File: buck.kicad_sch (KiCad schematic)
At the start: 0 parts

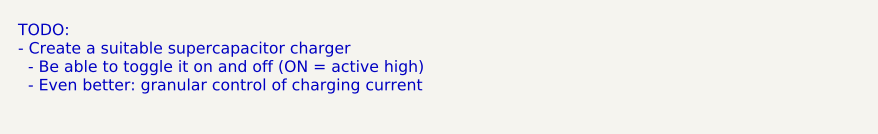
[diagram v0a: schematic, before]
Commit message: Add note about synchronous boost/buck needed
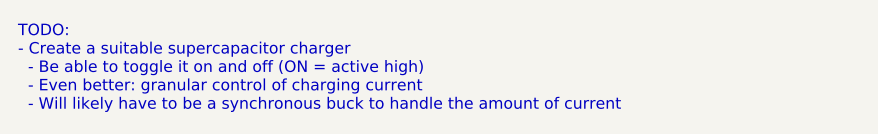
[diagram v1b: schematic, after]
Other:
- note added: "TODO: - Create a suitable supercapacitor charger - Be able to toggle it on and off (ON = active high) - Even better: granular control of charging current - Will likely have to be a synchronous buck to handle the amount of current"
- note removed: "TODO: - Create a suitable supercapacitor charger - Be able to toggle it on and off (ON = active high) - Even better: granular control of charging current"
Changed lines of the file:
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@@
 		(comment 1 "Robomaster")
 	)
-	(text "TODO:\n- Create a suitable supercapacitor charger\n  - Be able to toggle it on and off (ON = active high)\n  - Even better: granular control of charging current"
+	(text "TODO:\n- Create a suitable supercapacitor charger\n  - Be able to toggle it on and off (ON = active high)\n  - Even better: granular control of charging current\n  - Will likely have to be a synchronous buck to handle the amount of current"
 		(exclude_from_sim no)
 		(at 132.08 95.25 0)

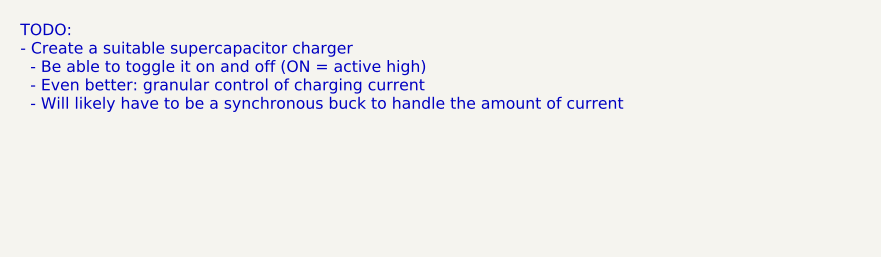
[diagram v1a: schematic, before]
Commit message: Added in & out data from each subsheet
For more details, please contact @leftisttachyon on Discord
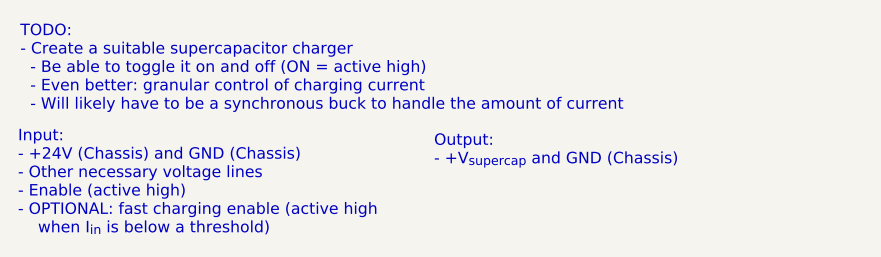
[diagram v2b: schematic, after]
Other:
- note added: "Input: - +24V (Chassis) and GND (Chassis) - Other necessary voltage lines - Enable (active high) - OPTIONAL: fast charging enable (active high when I_{in} is below a threshold)"
- note added: "Output: - +V_{supercap} and GND (Chassis)"
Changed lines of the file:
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@@
+		)
+	)
+	(text "Input:\n- +24V (Chassis) and GND (Chassis)\n- Other necessary voltage lines\n- Enable (active high)\n- OPTIONAL: fast charging enable (active high \n    when I_{in} is below a threshold)"
+		(exclude_from_sim no)
+		(at 131.826 106.934 0)
+		(effects
+			(font
+				(size 1.27 1.27)
+			)
+			(justify left top)
+		)
+	)
+	(text "Output:\n- +V_{supercap} and GND (Chassis)"
+		(exclude_from_sim no)
+		(at 178.054 107.442 0)
+		(effects
+			(font
+				(size 1.27 1.27)
+			)
+			(justify left top)
 		)
 	)

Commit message: Completed first version of housekeeping supplies
+5V and +3V3 from mini PC +24V
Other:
- company: UT Stampede -> UT Robomaster
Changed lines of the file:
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@@
 	(paper "A4")
 	(title_block
-		(date "2024-10-18")
+		(date "2024-11-15")
 		(rev "1")
-		(company "UT Stampede")
+		(company "UT Robomaster")
 		(comment 1 "Robomaster")
 	)

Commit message: Finishing buck charger
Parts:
- added C27: 0.1u, Capacitor_SMD:C_0603_1608Metric_Pad1.08x0.95mm_HandSolder, symbol Device:C_Small
- added C28, C31: 1u, Capacitor_SMD:C_0603_1608Metric_Pad1.08x0.95mm_HandSolder, symbol Device:C_Small
- added C29: 1u, Capacitor_SMD:C_0603_1608Metric_Pad1.08x0.95mm_HandSolder, symbol Device:C
- added C30: 2.2u, symbol Device:C_Polarized
- added C32, C33: 10u, symbol Device:C_Polarized
- added C34, C35: 0.1u, Capacitor_SMD:C_0603_1608Metric_Pad1.08x0.95mm_HandSolder, symbol Device:C
- added C36, C37: C, symbol Device:C_Polarized
- added C38: C, Capacitor_SMD:C_0603_1608Metric_Pad1.08x0.95mm_HandSolder, symbol Device:C
- added D3, D4: LED, LED_SMD:LED_0603_1608Metric_Pad1.05x0.95mm_HandSolder, symbol Device:LED
- added D5: BAT54J, Diode_SMD:D_SOD-323F, symbol Diode:BAT54J
- added L4: L, symbol Device:L
- added Q2, Q3: Q_NMOS_SGD, symbol Device:Q_NMOS_SGD
- added R17, R32, R35, R36: R, Resistor_SMD:R_0603_1608Metric_Pad0.98x0.95mm_HandSolder, symbol Device:R
- added R33: 6.8, Resistor_SMD:R_0603_1608Metric_Pad0.98x0.95mm_HandSolder, symbol Device:R
- added R34: 10m, Resistor_SMD:R_0603_1608Metric_Pad0.98x0.95mm_HandSolder, symbol Device:R
- added U9: BQ24640, ! Robomaster ICs:QFN50P350X350X100-17N-D, symbol ! Robomaster ICs:BQ24640
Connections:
- new net BTST: C27.1, D5.1 (K), U9.16 (BTST)
- new net CHARGE_EN: U9.2 (CE)
- new net GNDPWR: C28.2, C29.2, C30.2, C31.2, C32.2, C33.2, C34.2, C36.2, C37.2, Q3.1 (S), R36.2, U9.11 (GND), U9.17 (PAD)
- new net HIDRV: Q2.2 (G), U9.15 (HIDRV)
- new net IN: C30.1, C32.1, C33.1, Q2.3 (D), R17.1, R32.1, R33.1
- new net ISET: U9.7 (ISET)
- new net LODRV: Q3.2 (G), U9.13 (LODRV)
- new net OUT: C35.2, C36.1, C37.1, C38.1, R34.1, R35.1, U9.9 (SRN)
- new net PH: C27.2, L4.1, Q2.1 (S), Q3.3 (D), U9.14 (PH)
- new net REGN: C28.1, D5.2 (A), U9.12 (REGN)
- new net SRP: C34.1, C35.1, L4.2, R34.2, U9.10 (SRP)
- new net STAT: D3.1 (K), U9.3 (STAT)
- new net STAT_D: D3.2 (A), R17.2
- new net TS: U9.4 (TS)
- new net VCC: C29.1, R33.2, U9.1 (VCC)
- new net VFB: C38.2, R35.2, R36.1, U9.8 (VFB)
- new net VREF: C31.1, U9.6 (VREF)
- new net ~{PG}: D4.1 (K), U9.5 (~{PG})
- new net ~{PG}_D: D4.2 (A), R32.2
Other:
- note added: "Current sensing"
- note added: "Feedback network"
- note added: "High ESR"
- note added: "Low ESR"
- note added: "Output caps"
- note added: "Power path"
- note added: "Status LEDs for charging & current draw"
- note added: "Supercap Charging Controller"
- note added: "Totem pole"
- note added: "VCC Input Filtering"

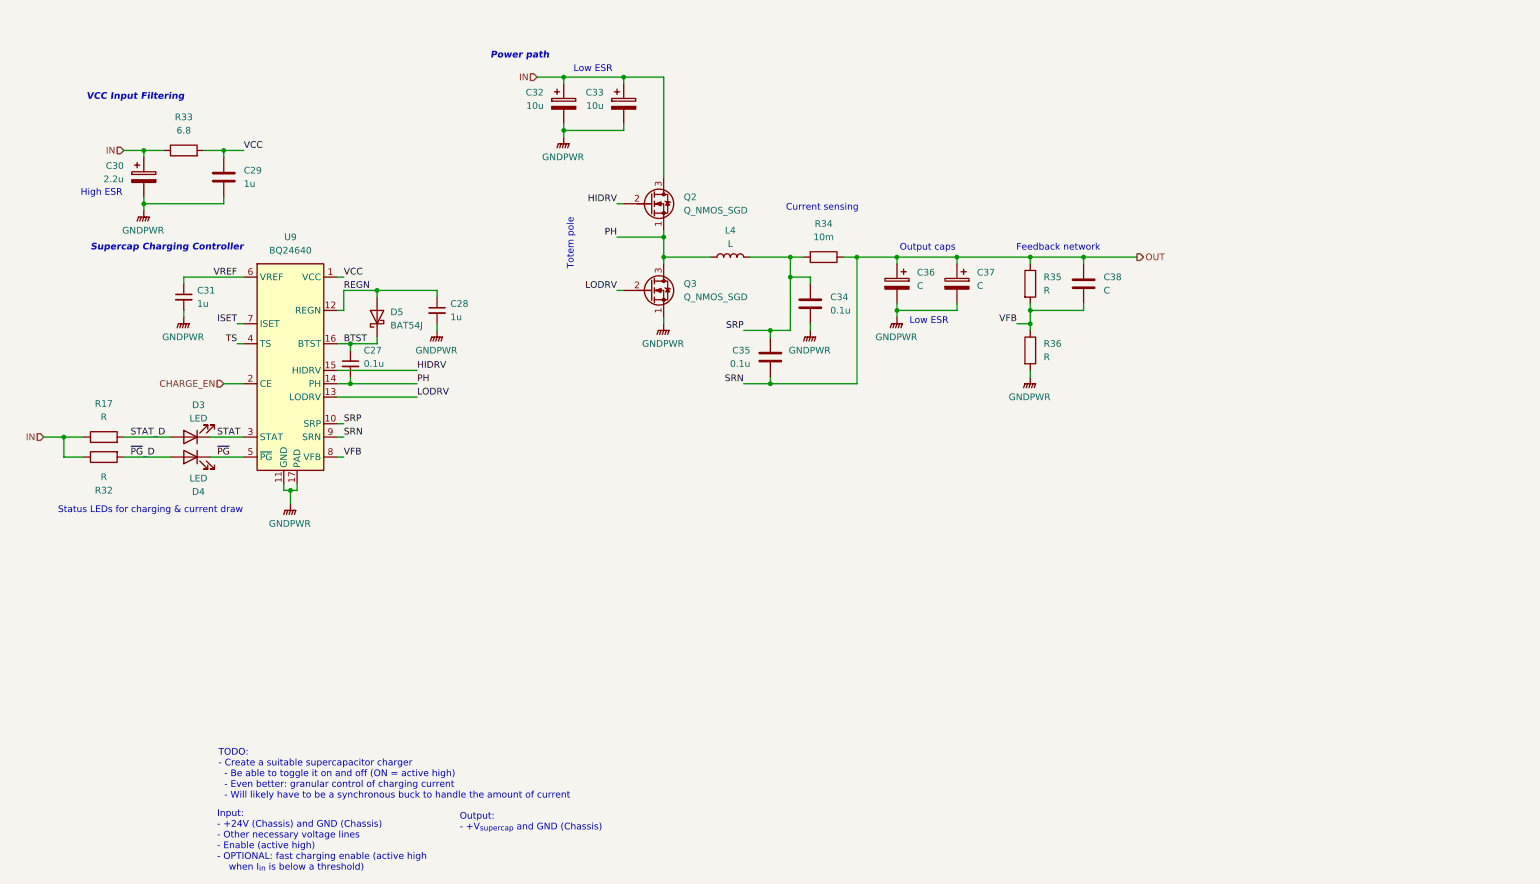
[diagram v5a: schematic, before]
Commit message: Define feedback networks
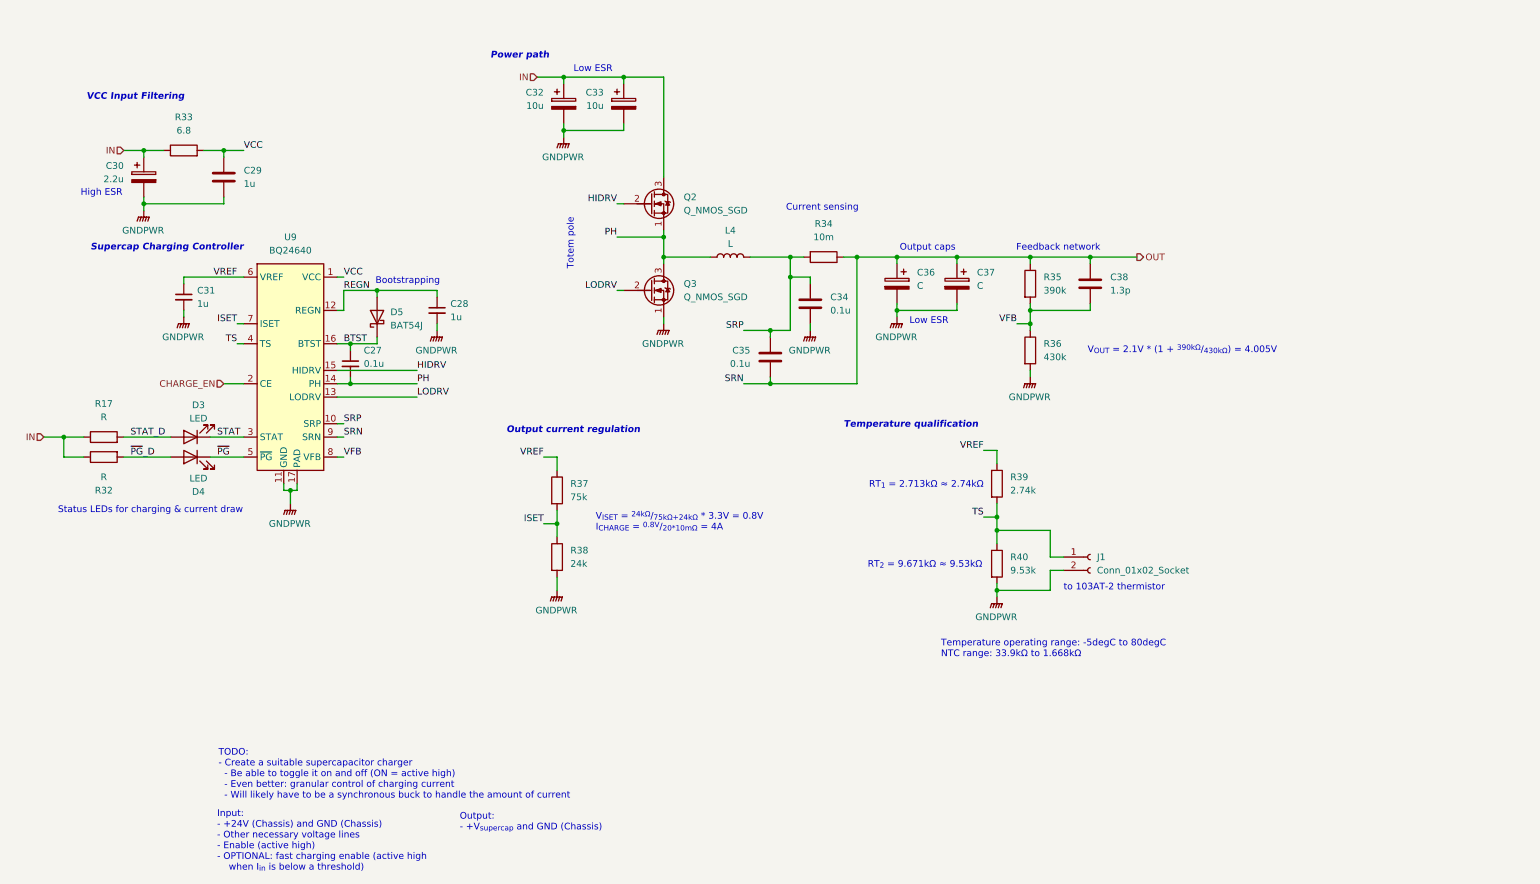
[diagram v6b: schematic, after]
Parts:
- added J1: Conn_01x02_Socket, Connector_PinSocket_2.00mm:PinSocket_1x02_P2.00mm_Vertical, symbol Connector:Conn_01x02_Socket
- added R37: 75k, Resistor_SMD:R_0603_1608Metric_Pad0.98x0.95mm_HandSolder, symbol Device:R
- added R38: 24k, Resistor_SMD:R_0603_1608Metric_Pad0.98x0.95mm_HandSolder, symbol Device:R
- added R39: 2.74k, Resistor_SMD:R_0603_1608Metric_Pad0.98x0.95mm_HandSolder, symbol Device:R
- added R40: 9.53k, Resistor_SMD:R_0603_1608Metric_Pad0.98x0.95mm_HandSolder, symbol Device:R
- C38: value C -> 1.3p
- R35: value R -> 390k
- R36: value R -> 430k
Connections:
- net GNDPWR: now also J1.2 (Pin_2), R38.2, R40.2
- net ISET: now also R37.2, R38.1
- net TS: now also J1.1 (Pin_1), R39.2, R40.1
- net VREF: now also R37.1, R39.1
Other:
- note added: "Bootstrapping"
- note added: "Output current regulation"
- note added: "RT_{1} = 2.713kΩ ≈ 2.74kΩ"
- note added: "RT_{2} = 9.671kΩ ≈ 9.53kΩ"
- note added: "Temperature operating range: -5degC to 80degC NTC range: 33.9kΩ to 1.668kΩ"
- note added: "Temperature qualification"
- note added: "V_{ISET} = ^{24kΩ}/_{75kΩ+24kΩ} * 3.3V = 0.8V I_{CHARGE} = ^{0.8V}/_{20*10mΩ} = 4A"
- note added: "V_{OUT} = 2.1V * (1 + ^{390kΩ}/_{430kΩ}) = 4.005V"
- note added: "to 103AT-2 thermistor"
- moved on the sheet: C38

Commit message: Finish up buck
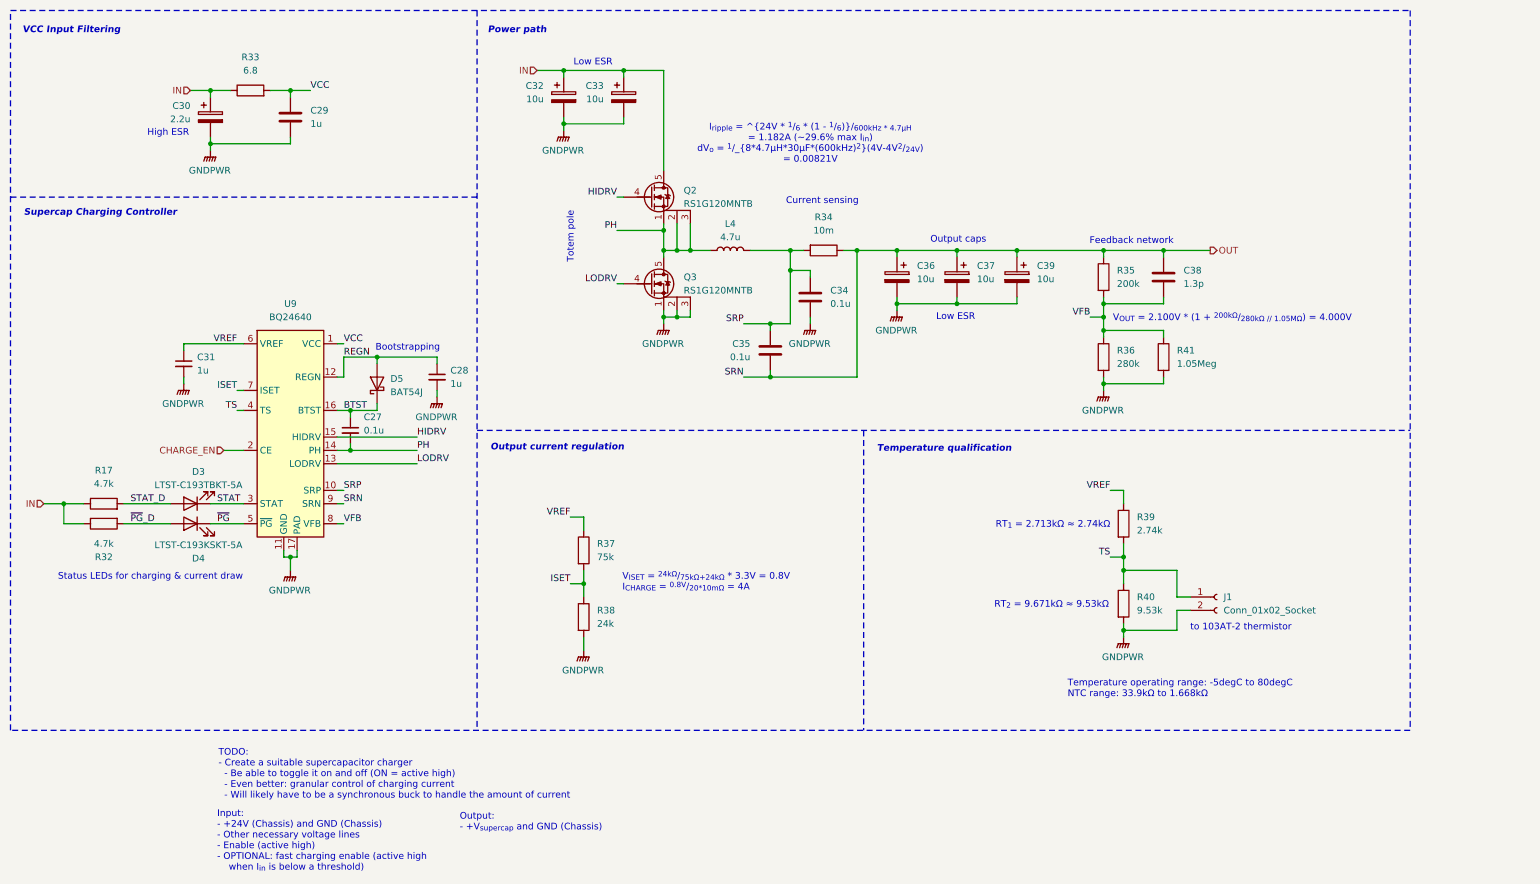
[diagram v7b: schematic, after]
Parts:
- added C39: 10u, Capacitor_THT:CP_Radial_D5.0mm_P2.00mm, symbol Device:C_Polarized
- added R41: 1.05Meg, Resistor_SMD:R_0603_1608Metric_Pad0.98x0.95mm_HandSolder, symbol Device:R
- C30: footprint (none) -> Capacitor_SMD:C_0603_1608Metric_Pad1.08x0.95mm_HandSolder
- C32, C33: footprint (none) -> Capacitor_THT:CP_Radial_D5.0mm_P2.00mm; Mouser Part Number (none) -> 598-106CKR063M
- C36, C37: value C -> 10u; footprint (none) -> Capacitor_THT:CP_Radial_D5.0mm_P2.00mm; Mouser Part Number (none) -> 598-106CKR063M
- D3: value LED -> LTST-C193TBKT-5A; Mouser Part Number (none) -> 859-LTSTC193TBKT5A
- D4: value LED -> LTST-C193KSKT-5A; Mouser Part Number (none) -> 859-LTSTC193KSKT5A
- L4: value L -> 4.7u
- Q2, Q3: value Q_NMOS_SGD -> RS1G120MNTB; footprint (none) -> Package_SO:PowerPAK_SO-8_Single; Mouser Part Number (none) -> 755-RS1G120MNTB
- R17, R32: value R -> 4.7k
- R35: value 390k -> 200k; Mouser Part Number (none) -> 667-ERA-3AEB204V
- R36: value 430k -> 280k; Mouser Part Number (none) -> 603-RT0603BRD07280KL
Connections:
- net GNDPWR: now also Q3.2 (S), Q3.3 (S), C39.2, R41.2
- net HIDRV: now also Q2.4 (G); no longer Q2.2 (G)
- net IN: now also Q2.5 (D); no longer Q2.3 (D)
- net LODRV: now also Q3.4 (G); no longer Q3.2 (G)
- net OUT: now also C39.1
- net PH: now also Q2.2 (S), Q2.3 (S), Q3.5 (D); no longer Q3.3 (D)
- net VFB: now also R41.1
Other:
- note added: "I_{ripple} = ^{24V * ^{1}/_{6} * (1 - ^{1}/_{6})}/_{600kHz * 4.7µH} = 1.182A (~29.6% max I_{in}) dV_{o} = ^{1}/_{8*4.7µH*30µF*(600kHz)^{2}}(4V-4V^{2}/_{24V}) = 0.00821V"
- note added: "V_{OUT} = 2.100V * (1 + ^{200kΩ}/_{280kΩ // 1.05MΩ}) = 4.000V"
- note removed: "V_{OUT} = 2.1V * (1 + ^{390kΩ}/_{430kΩ}) = 4.005V"
- moved on the sheet: C27, C28, C29, C30, C31, C32, C33, C34, C35, C36, C38, D3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

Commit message: Add global connectors
Also realize I messed up the current sense
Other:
- title: (none) -> Supercapacitor Charger
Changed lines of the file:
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@@
 	(paper "A4")
 	(title_block
+		(title "Supercapacitor Charger")
 		(date "2024-12-06")
 		(rev "1")
